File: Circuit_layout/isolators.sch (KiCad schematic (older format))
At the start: 36 parts, among them U17 MCP6004, U19 ACPL-C870, U20 ACPL-C870, U21 MCP6001

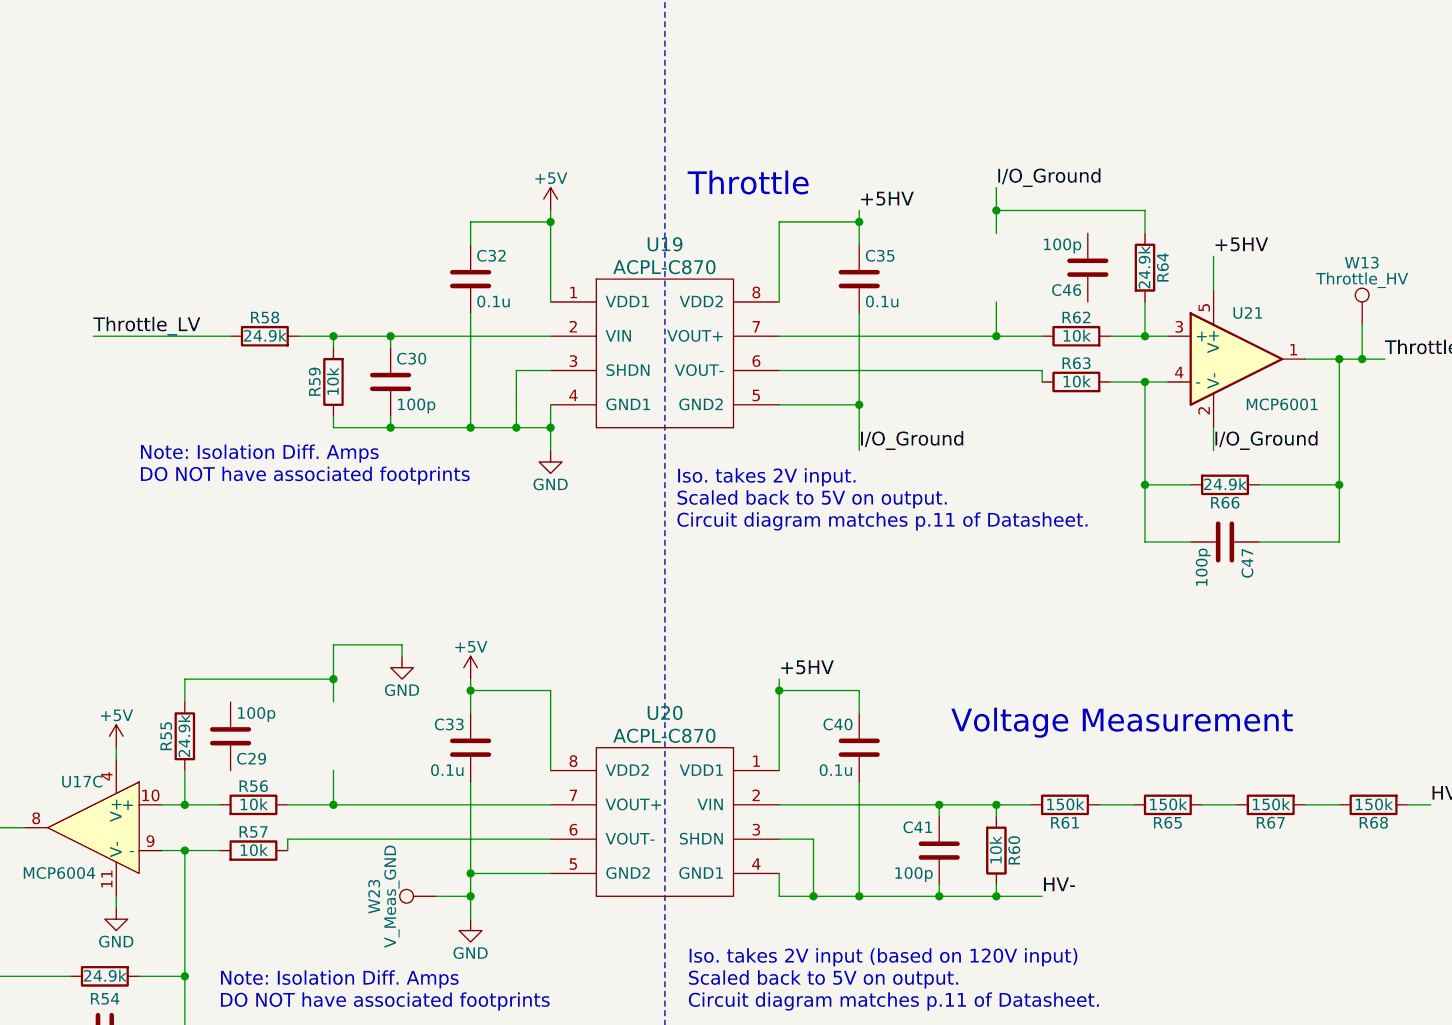
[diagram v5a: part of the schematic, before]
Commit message: made changes discussed in sch review w/ prof. added back +5 plane
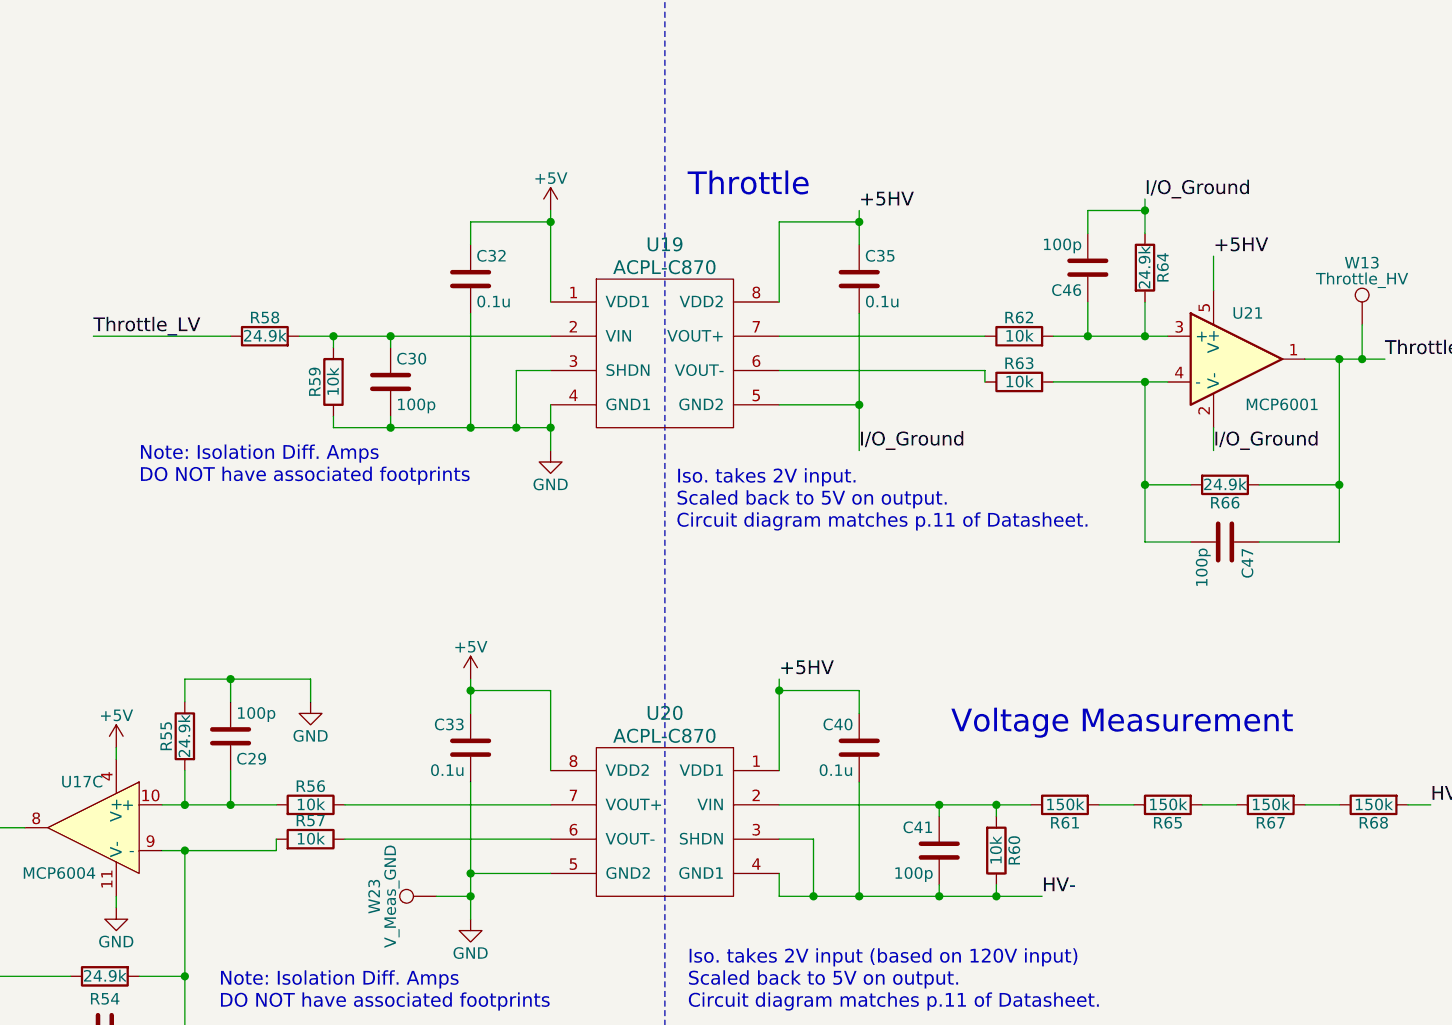
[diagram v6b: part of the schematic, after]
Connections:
- wire segments 98 -> 97
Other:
- moved on the sheet: R56, R57, R62, R63
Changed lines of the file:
@@
 V_Measure
 $Comp
-L GND #PWR0107
+L GND #PWR0103
 U 1 1 58B25770
 P 4950 3100
-F 0 "#PWR0107" H 4950 2850 50  0001 C CNN
+F 0 "#PWR0103" H 4950 2850 50  0001 C CNN
 F 1 "GND" H 4950 2950 50  0000 C CNN
 F 2 "" H 4950 3100 50  0000 C CNN
@@
 $EndComp
 $Comp
-L +5V #PWR0108
+L +5V #PWR0104
 U 1 1 58B257CF
 P 4950 2050
-F 0 "#PWR0108" H 4950 1900 50  0001 C CNN
+F 0 "#PWR0104" H 4950 1900 50  0001 C CNN
 F 1 "+5V" H 4950 2190 50  0000 C CNN
 F 2 "" H 4950 2050 50  0000 C CNN
@@
 Text Label 1400 1100 0    60   ~ 0
 I/O_Ground
-Text Label 6900 1950 0    60   ~ 0
+Text Label 7550 2000 0    60   ~ 0
 I/O_Ground
 Text Label 1300 800  0    60   ~ 0
@@
 L R R62
 U 1 1 58BC61A7
-P 7250 2600
-F 0 "R62" V 7330 2600 50  0000 C CNN
-F 1 "10k" V 7250 2600 50  0000 C CNN
-F 2 "Resistors_SMD:R_0805_HandSoldering" V 7180 2600 50  0001 C CNN
-F 3 "" H 7250 2600 50  0000 C CNN
-F 4 "P10.0KCCT-ND" V 7250 2600 60  0001 C CNN "DigiKey P/N"
-F 5 "http://www.digikey.com/product-detail/en/panasonic-electronic-components/ERJ-6ENF1002V/P10.0KCCT-ND/119248" V 7250 2600 60  0001 C CNN "URL"
-F 6 "ERJ-6ENF1002V" V 7250 2600 60  0001 C CNN "Man P/N"
-	1    7250 2600
+P 7000 2600
+F 0 "R62" V 7080 2600 50  0000 C CNN
+F 1 "10k" V 7000 2600 50  0000 C CNN
+F 2 "Resistors_SMD:R_0805_HandSoldering" V 6930 2600 50  0001 C CNN
+F 3 "" H 7000 2600 50  0000 C CNN
+F 4 "P10.0KCCT-ND" V 7000 2600 60  0001 C CNN "DigiKey P/N"
+F 5 "http://www.digikey.com/product-detail/en/panasonic-electronic-components/ERJ-6ENF1002V/P10.0KCCT-ND/119248" V 7000 2600 60  0001 C CNN "URL"
+F 6 "ERJ-6ENF1002V" V 7000 2600 60  0001 C CNN "Man P/N"
+	1    7000 2600
 	0    -1   -1   0
 $EndComp
@@
 L R R63
 U 1 1 58BC628C
-P 7250 2800
-F 0 "R63" V 7330 2800 50  0000 C CNN
-F 1 "10k" V 7250 2800 50  0000 C CNN
-F 2 "Resistors_SMD:R_0805_HandSoldering" V 7180 2800 50  0001 C CNN
-F 3 "" H 7250 2800 50  0000 C CNN
-F 4 "P10.0KCCT-ND" V 7250 2800 60  0001 C CNN "DigiKey P/N"
-F 5 "http://www.digikey.com/product-detail/en/panasonic-electronic-components/ERJ-6ENF1002V/P10.0KCCT-ND/119248" V 7250 2800 60  0001 C CNN "URL"
-F 6 "ERJ-6ENF1002V" V 7250 2800 60  0001 C CNN "Man P/N"
-	1    7250 2800
+P 7000 2800
+F 0 "R63" V 7080 2800 50  0000 C CNN
+F 1 "10k" V 7000 2800 50  0000 C CNN
+F 2 "Resistors_SMD:R_0805_HandSoldering" V 6930 2800 50  0001 C CNN
+F 3 "" H 7000 2800 50  0000 C CNN
+F 4 "P10.0KCCT-ND" V 7000 2800 60  0001 C CNN "DigiKey P/N"
+F 5 "http://www.digikey.com/product-detail/en/panasonic-electronic-components/ERJ-6ENF1002V/P10.0KCCT-ND/119248" V 7000 2800 60  0001 C CNN "URL"
+F 6 "ERJ-6ENF1002V" V 7000 2800 60  0001 C CNN "Man P/N"
+	1    7000 2800
 	0    -1   -1   0
 $EndComp
@@
 	7550 2800 7550 3500
 Wire Wire Line
-	7400 2800 7650 2800
+	7150 2800 7650 2800
 Wire Wire Line
 	8400 2700 8400 3500
@@
 Connection ~ 7550 2800
 Wire Wire Line
-	7400 2600 7650 2600
-Wire Wire Line
-	6900 2600 6900 2450
-Connection ~ 6900 2600
+	7150 2600 7650 2600
 Wire Wire Line
 	7550 2600 7550 2450
 Connection ~ 7550 2600
 Wire Wire Line
-	7550 2050 7550 2150
+	7550 2000 7550 2150
 Connection ~ 4000 2600
 Wire Wire Line
@@
 Wire Wire Line
 	2950 2600 3550 2600
-Wire Wire Line
-	5950 2600 7100 2600
 Wire Wire Line
 	1150 1450 1300 1450
@@
 	-1   0    0    1
 $EndComp
-Wire Wire Line
-	6900 1950 6900 2150
-Wire Wire Line
-	7550 2050 6900 2050
-Connection ~ 6900 2050
-Wire Wire Line
-	5950 2750 7100 2750
-Wire Wire Line
-	7100 2750 7100 2800
 Text Notes 5500 3450 0    60   ~ 0
 Iso. takes 2V input. \nScaled back to 5V on output.\nCircuit diagram matches p.11 of Datasheet.
@@
 +5HV
 $Comp
-L GND #PWR0109
+L GND #PWR0105
 U 1 1 58BC957F
 P 4600 5150
-F 0 "#PWR0109" H 4600 4900 50  0001 C CNN
+F 0 "#PWR0105" H 4600 4900 50  0001 C CNN
 F 1 "GND" H 4600 5000 50  0000 C CNN
 F 2 "" H 4600 5150 50  0000 C CNN
@@
 $EndComp
 $Comp
-L +5V #PWR0110
+L +5V #PWR0106
 U 1 1 58BC9585
 P 4600 4100
-F 0 "#PWR0110" H 4600 3950 50  0001 C CNN
+F 0 "#PWR0106" H 4600 3950 50  0001 C CNN
 F 1 "+5V" H 4600 4240 50  0000 C CNN
 F 2 "" H 4600 4100 50  0000 C CNN
@@
 L R R56
 U 1 1 58BC95D9
-P 3650 4650
-F 0 "R56" V 3730 4650 50  0000 C CNN
-F 1 "10k" V 3650 4650 50  0000 C CNN
-F 2 "Resistors_SMD:R_0805_HandSoldering" V 3580 4650 50  0001 C CNN
-F 3 "" H 3650 4650 50  0000 C CNN
-F 4 "P10.0KCCT-ND" V 3650 4650 60  0001 C CNN "DigiKey P/N"
-F 5 "http://www.digikey.com/product-detail/en/panasonic-electronic-components/ERJ-6ENF1002V/P10.0KCCT-ND/119248" V 3650 4650 60  0001 C CNN "URL"
-F 6 "ERJ-6ENF1002V" V 3650 4650 60  0001 C CNN "Man P/N"
-	1    3650 4650
+P 3900 4650
+F 0 "R56" V 3980 4650 50  0000 C CNN
+F 1 "10k" V 3900 4650 50  0000 C CNN
+F 2 "Resistors_SMD:R_0805_HandSoldering" V 3830 4650 50  0001 C CNN
+F 3 "" H 3900 4650 50  0000 C CNN
+F 4 "P10.0KCCT-ND" V 3900 4650 60  0001 C CNN "DigiKey P/N"
+F 5 "http://www.digikey.com/product-detail/en/panasonic-electronic-components/ERJ-6ENF1002V/P10.0KCCT-ND/119248" V 3900 4650 60  0001 C CNN "URL"
+F 6 "ERJ-6ENF1002V" V 3900 4650 60  0001 C CNN "Man P/N"
+	1    3900 4650
 	0    1    -1   0
 $EndComp
@@
 L R R57
 U 1 1 58BC95E2
-P 3650 4850
-F 0 "R57" V 3730 4850 50  0000 C CNN
-F 1 "10k" V 3650 4850 50  0000 C CNN
-F 2 "Resistors_SMD:R_0805_HandSoldering" V 3580 4850 50  0001 C CNN
-F 3 "" H 3650 4850 50  0000 C CNN
-F 4 "P10.0KCCT-ND" V 3650 4850 60  0001 C CNN "DigiKey P/N"
-F 5 "http://www.digikey.com/product-detail/en/panasonic-electronic-components/ERJ-6ENF1002V/P10.0KCCT-ND/119248" V 3650 4850 60  0001 C CNN "URL"
-F 6 "ERJ-6ENF1002V" V 3650 4850 60  0001 C CNN "Man P/N"
-	1    3650 4850
+P 3900 4800
+F 0 "R57" V 3980 4800 50  0000 C CNN
+F 1 "10k" V 3900 4800 50  0000 C CNN
+F 2 "Resistors_SMD:R_0805_HandSoldering" V 3830 4800 50  0001 C CNN
+F 3 "" H 3900 4800 50  0000 C CNN
+F 4 "P10.0KCCT-ND" V 3900 4800 60  0001 C CNN "DigiKey P/N"
+F 5 "http://www.digikey.com/product-detail/en/panasonic-electronic-components/ERJ-6ENF1002V/P10.0KCCT-ND/119248" V 3900 4800 60  0001 C CNN "URL"
+F 6 "ERJ-6ENF1002V" V 3900 4800 60  0001 C CNN "Man P/N"
+	1    3900 4800
 	0    1    -1   0
 $EndComp
@@
 	3350 4850 3350 5650
 Wire Wire Line
-	3250 4850 3500 4850
+	3250 4850 3750 4850
 Wire Wire Line
 	2500 4750 2500 5650
@@
 Connection ~ 3350 4850
 Wire Wire Line
-	3250 4650 3500 4650
-Wire Wire Line
-	4000 4650 4000 4500
-Connection ~ 4000 4650
+	3250 4650 3750 4650
 Wire Wire Line
 	3350 4650 3350 4500
@@
 Wire Wire Line
 	5950 4650 7050 4650
-Wire Wire Line
-	3800 4650 4950 4650
 Wire Wire Line
 	1400 5100 1400 4900
@@
 	1    0    0    1
 $EndComp
-Wire Wire Line
-	4000 3950 4000 4200
-Wire Wire Line
-	3350 4100 4000 4100
-Connection ~ 4000 4100
-Wire Wire Line
-	4950 4800 3800 4800
-Wire Wire Line
-	3800 4800 3800 4850
 Text Notes 5550 5550 0    60   ~ 0
 Iso. takes 2V input (based on 120V input)\nScaled back to 5V on output.\nCircuit diagram matches p.11 of Datasheet.
@@
 $EndComp
 $Comp
-L +5V #PWR0111
+L +5V #PWR0107
 U 1 1 58BCCFD7
 P 3050 4400
-F 0 "#PWR0111" H 3050 4250 50  0001 C CNN
+F 0 "#PWR0107" H 3050 4250 50  0001 C CNN
 F 1 "+5V" H 3050 4540 50  0000 C CNN
 F 2 "" H 3050 4400 50  0000 C CNN
@@
 	2850 5400 2500 5400
 Connection ~ 2500 5400
-Wire Wire Line
-	4000 3950 4300 3950
-Wire Wire Line
-	4300 3950 4300 4000
-$Comp
-L +5V #PWR0112
+$Comp
+L +5V #PWR0108
 U 1 1 58BCDEB7
 P 1400 4450
-F 0 "#PWR0112" H 1400 4300 50  0001 C CNN
+F 0 "#PWR0108" H 1400 4300 50  0001 C CNN
 F 1 "+5V" H 1400 4590 50  0000 C CNN
 F 2 "" H 1400 4450 50  0000 C CNN
@@
 $EndComp
 $Comp
-L GND #PWR0113
+L GND #PWR0109
 U 1 1 58BCDF52
 P 1400 5100
-F 0 "#PWR0113" H 1400 4850 50  0001 C CNN
+F 0 "#PWR0109" H 1400 4850 50  0001 C CNN
 F 1 "GND" H 1400 4950 50  0000 C CNN
 F 2 "" H 1400 5100 50  0000 C CNN
@@
 Connection ~ 2300 4750
 $Comp
-L GND #PWR0114
+L GND #PWR0110
 U 1 1 58D08937
-P 4300 4000
-F 0 "#PWR0114" H 4300 3750 50  0001 C CNN
-F 1 "GND" H 4300 3850 50  0000 C CNN
-F 2 "" H 4300 4000 50  0000 C CNN
-F 3 "" H 4300 4000 50  0000 C CNN
-	1    4300 4000
+P 3900 4200
+F 0 "#PWR0110" H 3900 3950 50  0001 C CNN
+F 1 "GND" H 3900 4050 50  0000 C CNN
+F 2 "" H 3900 4200 50  0000 C CNN
+F 3 "" H 3900 4200 50  0000 C CNN
+	1    3900 4200
 	-1   0    0    -1
 $EndComp
@@
 	3050 5050 3050 5100
 $Comp
-L GND #PWR0115
+L GND #PWR0111
 U 1 1 58D09DC0
 P 3050 5100
-F 0 "#PWR0115" H 3050 4850 50  0001 C CNN
+F 0 "#PWR0111" H 3050 4850 50  0001 C CNN
 F 1 "GND" H 3050 4950 50  0000 C CNN
 F 2 "" H 3050 5100 50  0000 C CNN
@@
 	0    -1   -1   0
 $EndComp
+Wire Wire Line
+	7300 2450 7300 2600
+Connection ~ 7300 2600
+Wire Wire Line
+	7300 2150 7300 2050
+Wire Wire Line
+	7300 2050 7550 2050
+Connection ~ 7550 2050
+Wire Wire Line
+	5950 2750 6850 2750
+Wire Wire Line
+	6850 2750 6850 2800
+Wire Wire Line
+	5950 2600 6850 2600
+Wire Wire Line
+	3750 4850 3750 4800
+Wire Wire Line
+	3550 4500 3550 4650
+Connection ~ 3550 4650
+Wire Wire Line
+	3550 4200 3550 4100
+Wire Wire Line
+	4050 4650 4950 4650
+Wire Wire Line
+	4050 4800 4950 4800
+Wire Wire Line
+	3900 4100 3900 4200
+Wire Wire Line
+	3350 4100 3900 4100
+Connection ~ 3550 4100
 $EndSCHEMATC

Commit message: organized sheet more, updated some footprints
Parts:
- removed C27: 0.1u, Capacitors_SMD:C_0805_HandSoldering, symbol C
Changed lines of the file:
@@
 V_Measure
 $Comp
-L GND #PWR0103
+L GND #PWR0101
 U 1 1 58B25770
 P 4950 3100
-F 0 "#PWR0103" H 4950 2850 50  0001 C CNN
+F 0 "#PWR0101" H 4950 2850 50  0001 C CNN
 F 1 "GND" H 4950 2950 50  0000 C CNN
 F 2 "" H 4950 3100 50  0000 C CNN
@@
 $EndComp
 $Comp
-L +5V #PWR0104
+L +5V #PWR0102
 U 1 1 58B257CF
 P 4950 2050
-F 0 "#PWR0104" H 4950 1900 50  0001 C CNN
+F 0 "#PWR0102" H 4950 1900 50  0001 C CNN
 F 1 "+5V" H 4950 2190 50  0000 C CNN
 F 2 "" H 4950 2050 50  0000 C CNN
@@
 +5HV
 $Comp
-L GND #PWR0105
+L GND #PWR0103
 U 1 1 58BC957F
 P 4600 5150
-F 0 "#PWR0105" H 4600 4900 50  0001 C CNN
+F 0 "#PWR0103" H 4600 4900 50  0001 C CNN
 F 1 "GND" H 4600 5000 50  0000 C CNN
 F 2 "" H 4600 5150 50  0000 C CNN
@@
 $EndComp
 $Comp
-L +5V #PWR0106
+L +5V #PWR0104
 U 1 1 58BC9585
 P 4600 4100
-F 0 "#PWR0106" H 4600 3950 50  0001 C CNN
+F 0 "#PWR0104" H 4600 3950 50  0001 C CNN
 F 1 "+5V" H 4600 4240 50  0000 C CNN
 F 2 "" H 4600 4100 50  0000 C CNN
@@
 F 6 "ACPL-C870-000E" H 5450 4450 60  0001 C CNN "Man P/N"
 	1    5450 4450
-	-1   0    0    -1
-$EndComp
-$Comp
-L C C27
-U 1 1 58BC95A1
-P 1400 4750
-F 0 "C27" H 1425 4850 50  0000 L CNN
-F 1 "0.1u" H 1425 4650 50  0000 L CNN
-F 2 "Capacitors_SMD:C_0805_HandSoldering" H 1438 4600 50  0001 C CNN
-F 3 "http://www.kemet.com/Lists/ProductCatalog/Attachments/53/KEM_C1002_X7R_SMD.pdf" H 1400 4750 50  0001 C CNN
-F 4 "399-1168-1-ND" H 1400 4750 60  0001 C CNN "Digikey P/N"
-F 5 "http://www.digikey.com/product-detail/en/kemet/C0805C104K3RACTU/399-1168-1-ND/411443" H 1400 4750 60  0001 C CNN "URL"
-F 6 "C0805C104K3RACTU" H 1400 4750 60  0001 C CNN "Man P/N"
-	1    1400 4750
 	-1   0    0    -1
 $EndComp
@@
 	5950 4650 7050 4650
 Wire Wire Line
-	1400 5100 1400 4900
-Wire Wire Line
-	1400 4600 1400 4450
-Wire Wire Line
 	5950 4100 5950 4500
 Wire Wire Line
@@
 $EndComp
 $Comp
-L +5V #PWR0107
+L +5V #PWR0105
 U 1 1 58BCCFD7
 P 3050 4400
-F 0 "#PWR0107" H 3050 4250 50  0001 C CNN
+F 0 "#PWR0105" H 3050 4250 50  0001 C CNN
 F 1 "+5V" H 3050 4540 50  0000 C CNN
 F 2 "" H 3050 4400 50  0000 C CNN
@@
 	2850 5400 2500 5400
 Connection ~ 2500 5400
-$Comp
-L +5V #PWR0108
-U 1 1 58BCDEB7
-P 1400 4450
-F 0 "#PWR0108" H 1400 4300 50  0001 C CNN
-F 1 "+5V" H 1400 4590 50  0000 C CNN
-F 2 "" H 1400 4450 50  0000 C CNN
-F 3 "" H 1400 4450 50  0000 C CNN
-	1    1400 4450
-	-1   0    0    -1
-$EndComp
-$Comp
-L GND #PWR0109
-U 1 1 58BCDF52
-P 1400 5100
-F 0 "#PWR0109" H 1400 4850 50  0001 C CNN
-F 1 "GND" H 1400 4950 50  0000 C CNN
-F 2 "" H 1400 5100 50  0000 C CNN
-F 3 "" H 1400 5100 50  0000 C CNN
-	1    1400 5100
-	-1   0    0    -1
-$EndComp
 Connection ~ 6900 5050
 Wire Wire Line
@@
 Connection ~ 2300 4750
 $Comp
-L GND #PWR0110
+L GND #PWR0106
 U 1 1 58D08937
 P 3900 4200
-F 0 "#PWR0110" H 3900 3950 50  0001 C CNN
+F 0 "#PWR0106" H 3900 3950 50  0001 C CNN
 F 1 "GND" H 3900 4050 50  0000 C CNN
 F 2 "" H 3900 4200 50  0000 C CNN
@@
 	3050 5050 3050 5100
 $Comp
-L GND #PWR0111
+L GND #PWR0107
 U 1 1 58D09DC0
 P 3050 5100
-F 0 "#PWR0111" H 3050 4850 50  0001 C CNN
+F 0 "#PWR0107" H 3050 4850 50  0001 C CNN
 F 1 "GND" H 3050 4950 50  0000 C CNN
 F 2 "" H 3050 5100 50  0000 C CNN

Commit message: added more tracks
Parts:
- renumbered W14 to +5HV1, W15 to IO_GND1, W13 to Thrtl_HV1, W12 to V_Meas1, W23 to V_Meas_GND1
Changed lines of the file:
@@
 V_Measure
 $Comp
-L GND #PWR0101
+L GND #PWR0103
 U 1 1 58B25770
 P 4950 3100
-F 0 "#PWR0101" H 4950 2850 50  0001 C CNN
+F 0 "#PWR0103" H 4950 2850 50  0001 C CNN
 F 1 "GND" H 4950 2950 50  0000 C CNN
 F 2 "" H 4950 3100 50  0000 C CNN
@@
 $EndComp
 $Comp
-L +5V #PWR0102
+L +5V #PWR0104
 U 1 1 58B257CF
 P 4950 2050
-F 0 "#PWR0102" H 4950 1900 50  0001 C CNN
+F 0 "#PWR0104" H 4950 1900 50  0001 C CNN
 F 1 "+5V" H 4950 2190 50  0000 C CNN
 F 2 "" H 4950 2050 50  0000 C CNN
@@
 +5HV
 $Comp
-L GND #PWR0103
+L GND #PWR0105
 U 1 1 58BC957F
 P 4600 5150
-F 0 "#PWR0103" H 4600 4900 50  0001 C CNN
+F 0 "#PWR0105" H 4600 4900 50  0001 C CNN
 F 1 "GND" H 4600 5000 50  0000 C CNN
 F 2 "" H 4600 5150 50  0000 C CNN
@@
 $EndComp
 $Comp
-L +5V #PWR0104
+L +5V #PWR0106
 U 1 1 58BC9585
 P 4600 4100
-F 0 "#PWR0104" H 4600 3950 50  0001 C CNN
+F 0 "#PWR0106" H 4600 3950 50  0001 C CNN
 F 1 "+5V" H 4600 4240 50  0000 C CNN
 F 2 "" H 4600 4100 50  0000 C CNN
@@
 $EndComp
 $Comp
-L +5V #PWR0105
+L +5V #PWR0107
 U 1 1 58BCCFD7
 P 3050 4400
-F 0 "#PWR0105" H 3050 4250 50  0001 C CNN
+F 0 "#PWR0107" H 3050 4250 50  0001 C CNN
 F 1 "+5V" H 3050 4540 50  0000 C CNN
 F 2 "" H 3050 4400 50  0000 C CNN
@@
 	5450 7800 5450 450
 $Comp
-L TEST_1P W13
+L TEST_1P Thrtl_HV1
 U 1 1 58C2EF83
 P 8500 2550
-F 0 "W13" H 8500 2820 50  0000 C CNN
+F 0 "Thrtl_HV1" H 8500 2820 50  0000 C CNN
 F 1 "Throttle_HV" H 8500 2750 50  0000 C CNN
 F 2 "Measurement_Points:Measurement_Point_Round-SMD-Pad_Big" H 8700 2550 50  0001 C CNN
@@
 Connection ~ 8500 2700
 $Comp
-L TEST_1P W14
+L TEST_1P +5HV1
 U 1 1 58C2F5EA
 P 9500 2400
-F 0 "W14" H 9500 2670 50  0000 C CNN
+F 0 "+5HV1" H 9500 2670 50  0000 C CNN
 F 1 "+5HV" H 9500 2600 50  0000 C CNN
 F 2 "Measurement_Points:Measurement_Point_Round-SMD-Pad_Big" H 9700 2400 50  0001 C CNN
@@
 $EndComp
 $Comp
-L TEST_1P W15
+L TEST_1P IO_GND1
 U 1 1 58C2F6F4
 P 9500 2900
-F 0 "W15" H 9500 3170 50  0000 C CNN
+F 0 "IO_GND1" H 9500 3170 50  0000 C CNN
 F 1 "I/O_Ground" H 9500 3100 50  0000 C CNN
 F 2 "Measurement_Points:Measurement_Point_Round-SMD-Pad_Big" H 9700 2900 50  0001 C CNN
@@
 Connection ~ 9250 2900
 $Comp
-L TEST_1P W12
+L TEST_1P V_Meas1
 U 1 1 58C2FC1B
 P 2300 4600
-F 0 "W12" H 2300 4870 50  0000 C CNN
+F 0 "V_Meas1" H 2300 4870 50  0000 C CNN
 F 1 "V_Measure" H 2300 4800 50  0000 C CNN
 F 2 "Measurement_Points:Measurement_Point_Round-SMD-Pad_Big" H 2500 4600 50  0001 C CNN
@@
 Connection ~ 2300 4750
 $Comp
-L GND #PWR0106
+L GND #PWR0108
 U 1 1 58D08937
 P 3900 4200
-F 0 "#PWR0106" H 3900 3950 50  0001 C CNN
+F 0 "#PWR0108" H 3900 3950 50  0001 C CNN
 F 1 "GND" H 3900 4050 50  0000 C CNN
 F 2 "" H 3900 4200 50  0000 C CNN
@@
 	3050 5050 3050 5100
 $Comp
-L GND #PWR0107
+L GND #PWR0109
 U 1 1 58D09DC0
 P 3050 5100
-F 0 "#PWR0107" H 3050 4850 50  0001 C CNN
+F 0 "#PWR0109" H 3050 4850 50  0001 C CNN
 F 1 "GND" H 3050 4950 50  0000 C CNN
 F 2 "" H 3050 5100 50  0000 C CNN
@@
 Connection ~ 4600 5050
 $Comp
-L TEST_1P W23
+L TEST_1P V_Meas_GND1
 U 1 1 58D30357
 P 4450 5050
-F 0 "W23" H 4450 5320 50  0000 C CNN
+F 0 "V_Meas_GND1" H 4450 5320 50  0000 C CNN
 F 1 "V_Meas_GND" H 4450 5250 50  0000 C CNN
 F 2 "Measurement_Points:Measurement_Point_Square-SMD-Pad_Big" H 4650 5050 50  0001 C CNN
